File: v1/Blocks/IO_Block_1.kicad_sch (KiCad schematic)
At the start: 12 parts, among them IC1 TLP172AM_TPR,E, IC2 TLP172AM_TPR,E, IC3 TLP172AM_TPR,E, IC4 TLP172AM_TPR,E, IC5 TLP172AM_TPR,E, IC6 TLP172AM_TPR,E

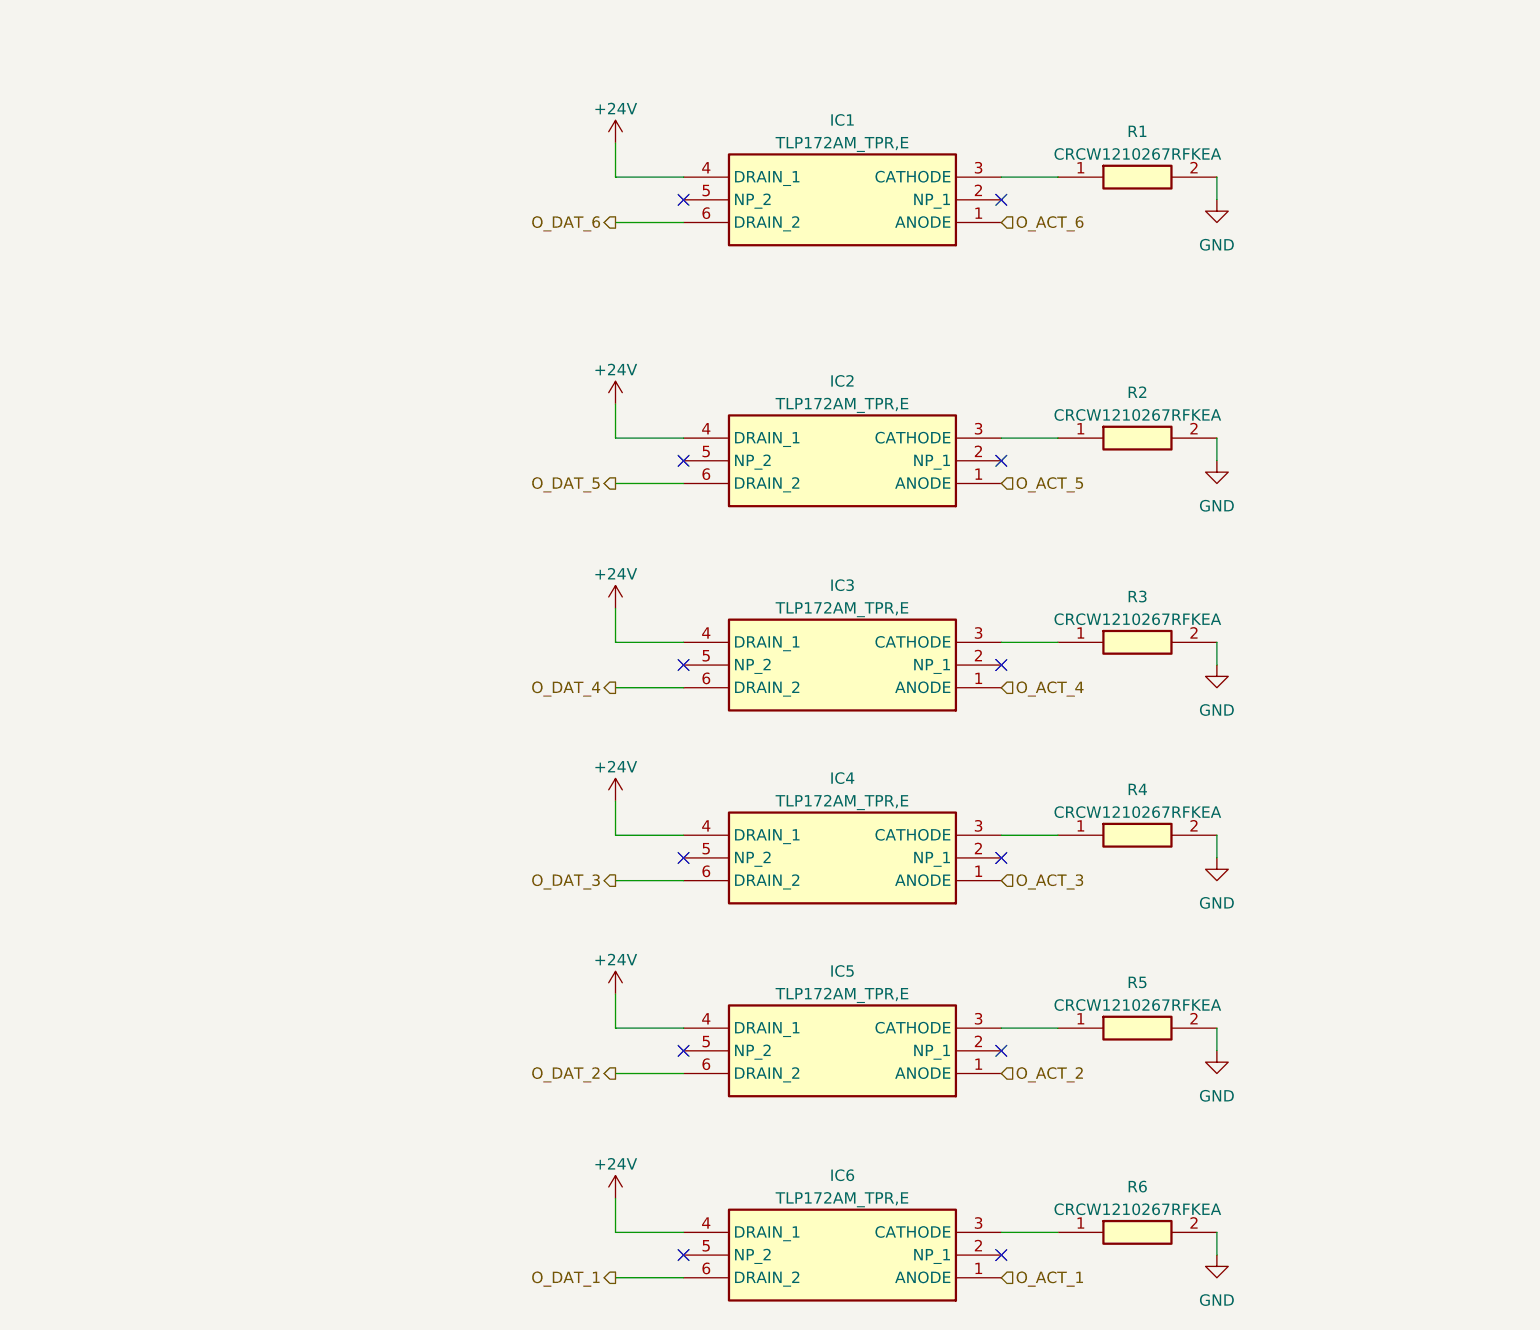
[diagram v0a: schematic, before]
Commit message: Update views, to make drawing sheets smaller where necessary
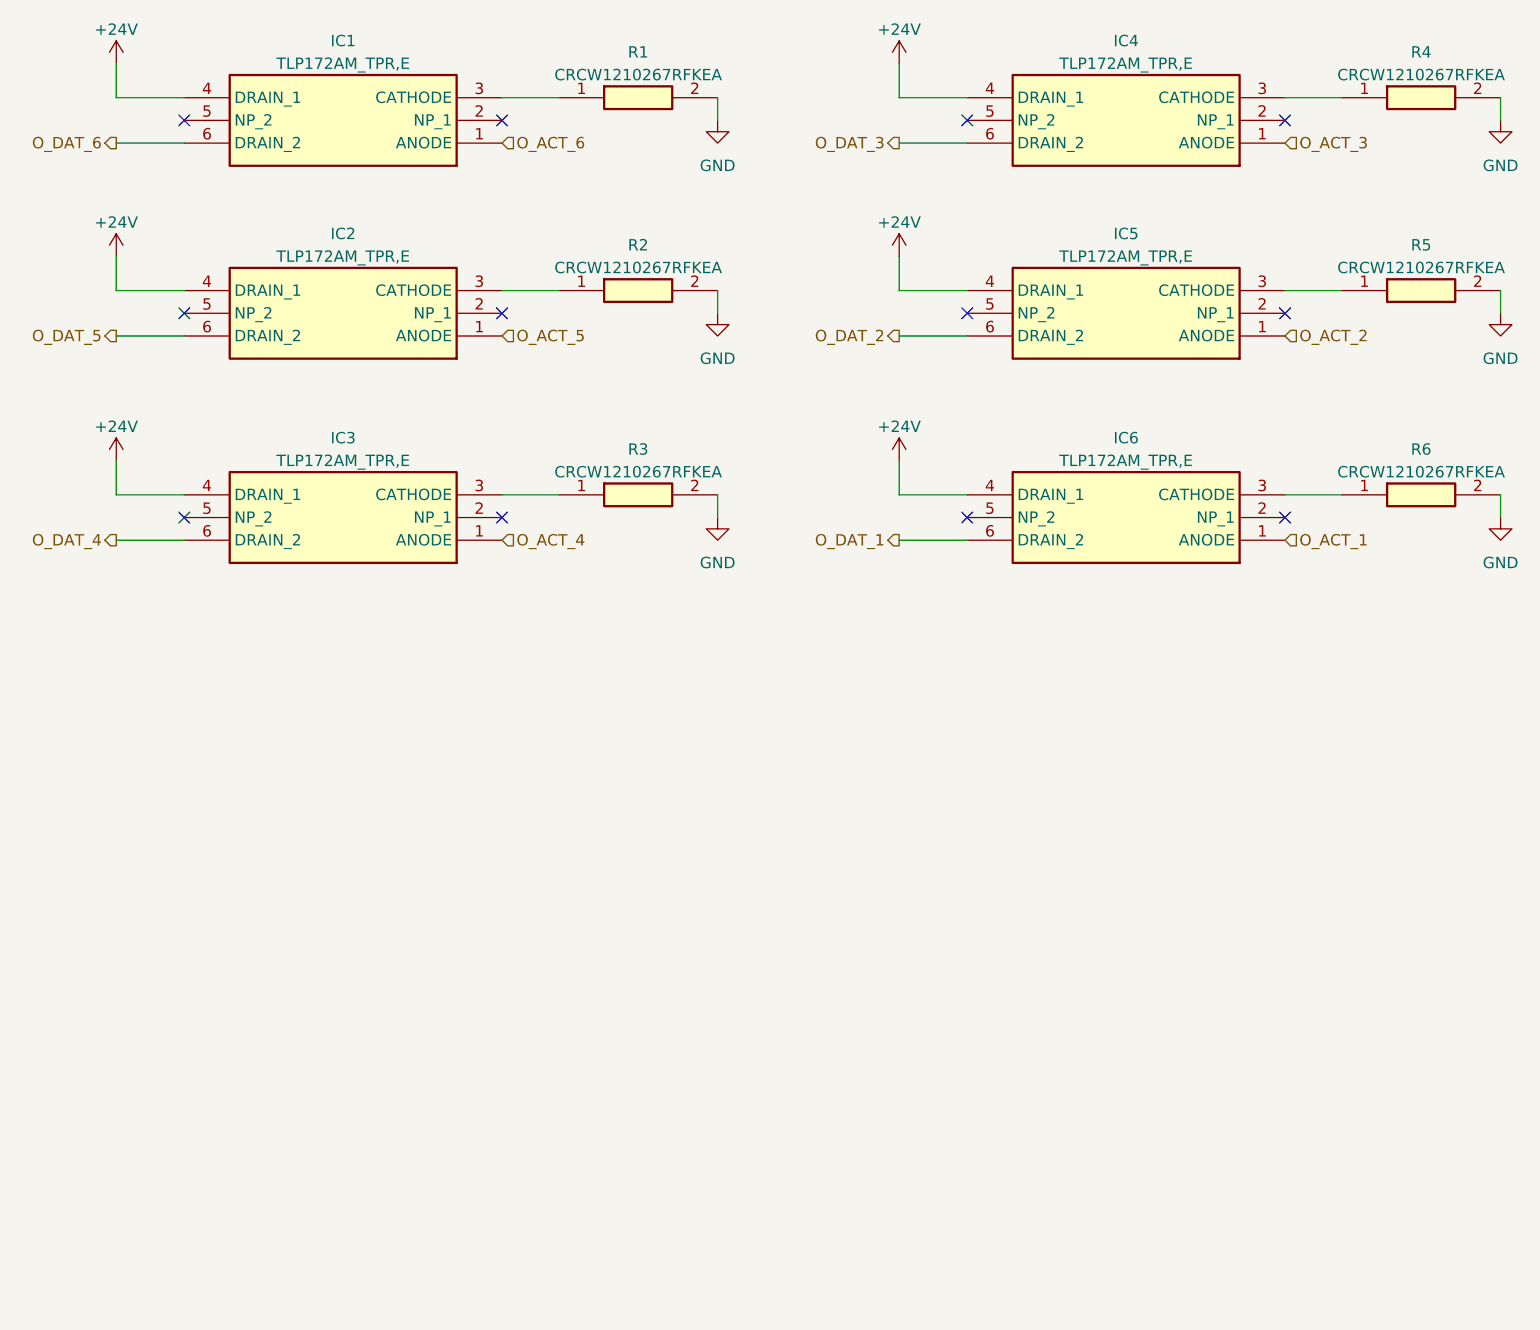
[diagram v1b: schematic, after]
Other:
- moved on the sheet: IC1, IC2, IC3, IC4, IC5, IC6, R1, R2, R3, R4, R5, R6
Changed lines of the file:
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@@
 (kicad_sch (version 20230121) (generator eeschema)
-  (paper "A4")
+  (paper "A5")
   (title_block
     (date "2023-04-23")
